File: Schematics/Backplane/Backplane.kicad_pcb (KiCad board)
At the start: 2 copper layers, 69.5 x 99 mm, 17 parts, among them J1 Edge Connector (SLOT 1), J2 Edge Connector (SLOT 2), J3 Edge Connector (SLOT 3), J4 Edge Connector (SLOT 4), J5 Edge Connector (SLOT 5)

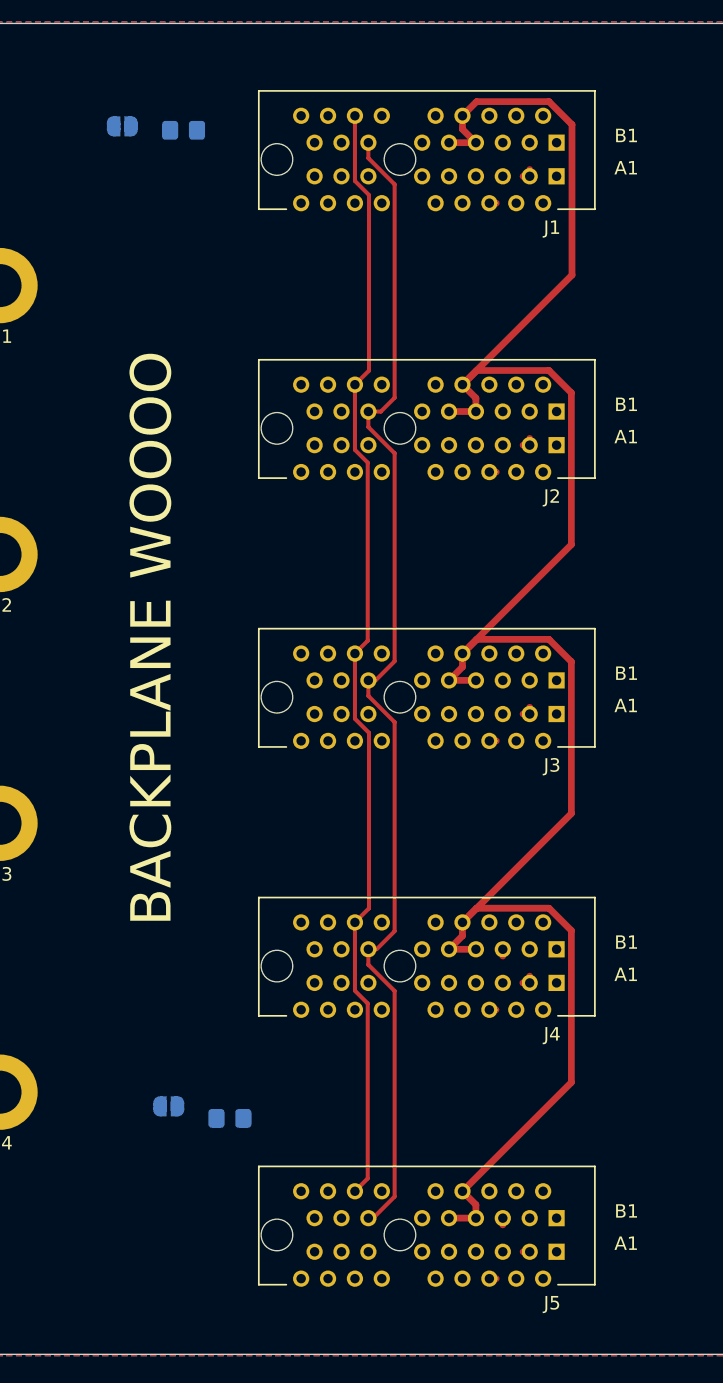
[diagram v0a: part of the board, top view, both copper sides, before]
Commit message: Tweaked slot placement on PCB
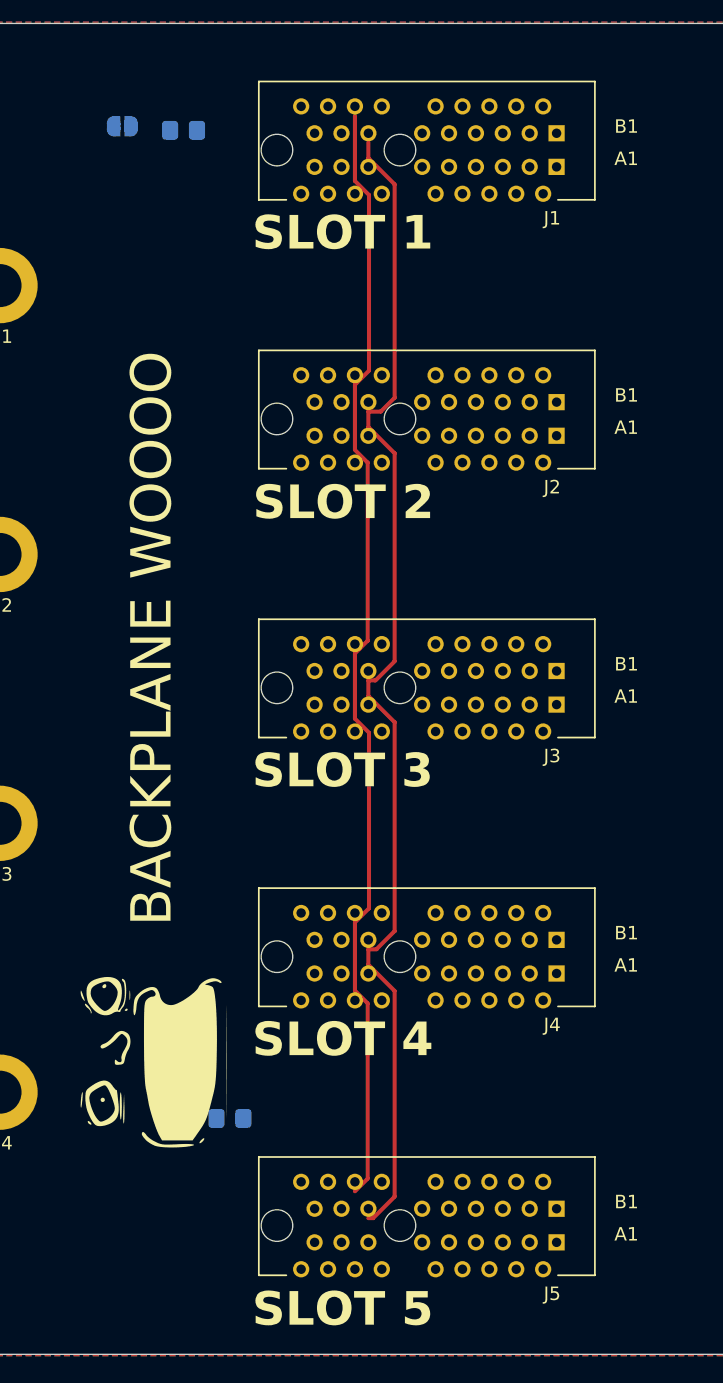
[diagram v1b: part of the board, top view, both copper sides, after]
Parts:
- moved J4 0.70 mm to (32.8, 69.4)
- moved J5 0.70 mm to (32.8, 89.4)
- moved J1 0.70 mm to (32.8, 9.42)
- moved J2 0.70 mm to (32.8, 29.4)
- moved J3 0.70 mm to (32.8, 49.4)
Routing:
- net BATT_B: track 150.0 -> 0.00 mm
- net GND1: track 8.00 -> 0.00 mm
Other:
- board text added: "SLOT 1"
- board text added: "SLOT 2"
- board text added: "SLOT 3"
- board text added: "SLOT 4"
- board text added: "SLOT 5"

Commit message: Best attempt at 2-layer PCB (incomplete)
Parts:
- removed JP1: TOP_TERMINATION, Jumper:SolderJumper-2_P1.3mm_Open_RoundedPad1.0x1.5mm
- removed JP2: BOT_TERMINATION, Jumper:SolderJumper-2_P1.3mm_Open_RoundedPad1.0x1.5mm
- R1: footprint Resistor_SMD:R_0805_2012Metric_Pad1.20x1.40mm_HandSolder -> Resistor_SMD:R_0603_1608Metric_Pad0.98x0.95mm_HandSolder
- R2: footprint Resistor_SMD:R_0805_2012Metric_Pad1.20x1.40mm_HandSolder -> Resistor_SMD:R_0603_1608Metric
- moved R2 6.97 mm to (19.6, 88.4)
- moved R1 2.56 mm to (19.2, 8.15)
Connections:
- net CAN_L renamed CAN_N
- J1 pad B14: CAN_H -> CAN_P
- J2 pad B14: CAN_H -> CAN_P
- J3 pad B14: CAN_H -> CAN_P
- J4 pad B14: CAN_H -> CAN_P
- J5 pad B14: CAN_H -> CAN_P
- R1 pad 1: Net-(JP1-A) -> CAN_P
- R2 pad 1: Net-(JP2-A) -> CAN_P
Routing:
- net BATT_B: track 0.00 -> 135.2 mm
- net 3.3V_A: track 0.00 -> 127.2 mm, vias 0 -> 4
- net GND1: track 0.00 -> 111.7 mm
- net BATT_A: track 0.00 -> 84.2 mm
- net CAN_H: track 83.3 -> 0.00 mm
- net 5.0V_A: track 0.00 -> 74.3 mm, vias 0 -> 2
- net GND2: track 0.00 -> 73.2 mm
- net 3.3V_B: track 0.00 -> 57.8 mm
- net CAN_N: track 87.9 -> 59.8 mm
- net CAN_P: track 0.00 -> 21.2 mm
- removed copper zone on F.Cu, net GND1
- removed copper zone on B.Cu, net GND2
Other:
- copper layers 2 -> 4
- board text added: "Don't use full copper pours; want PCB to be as RF-penetrable as possible"
- board text added: "MODULARIZED SYSTEMS INTERCONNECTED IN VERTICAL STACK (MSIVS) Acronym; something that describes the connected yet independent module stack"
- board text added: "Make sure to use busbars; don't want current to have to run through each connector to get from SLOT1 to SLOT5"
- board text added: "STACK INTERCONNECT GEN1"
- board text added: "Very likely going to need to do 4-layer"

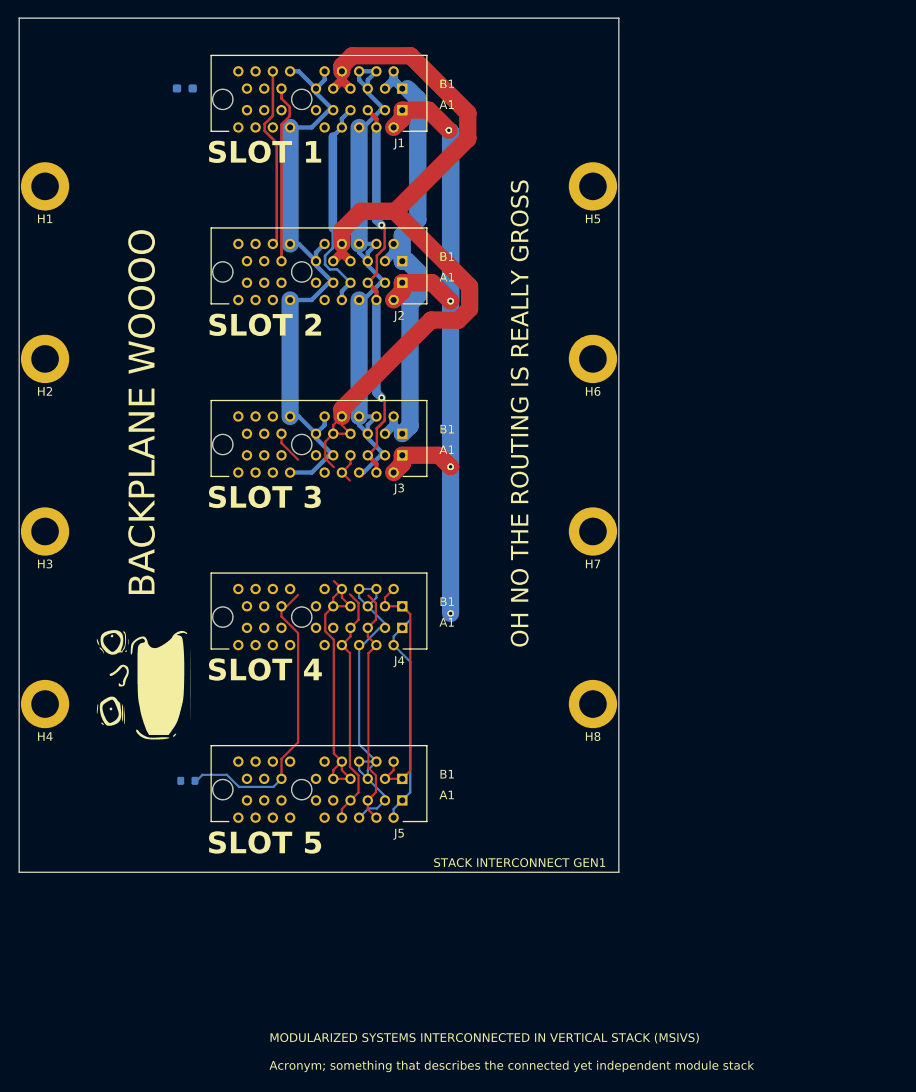
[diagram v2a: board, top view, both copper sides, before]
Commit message: Completed PCB layout (2-layer). DRC Pass.
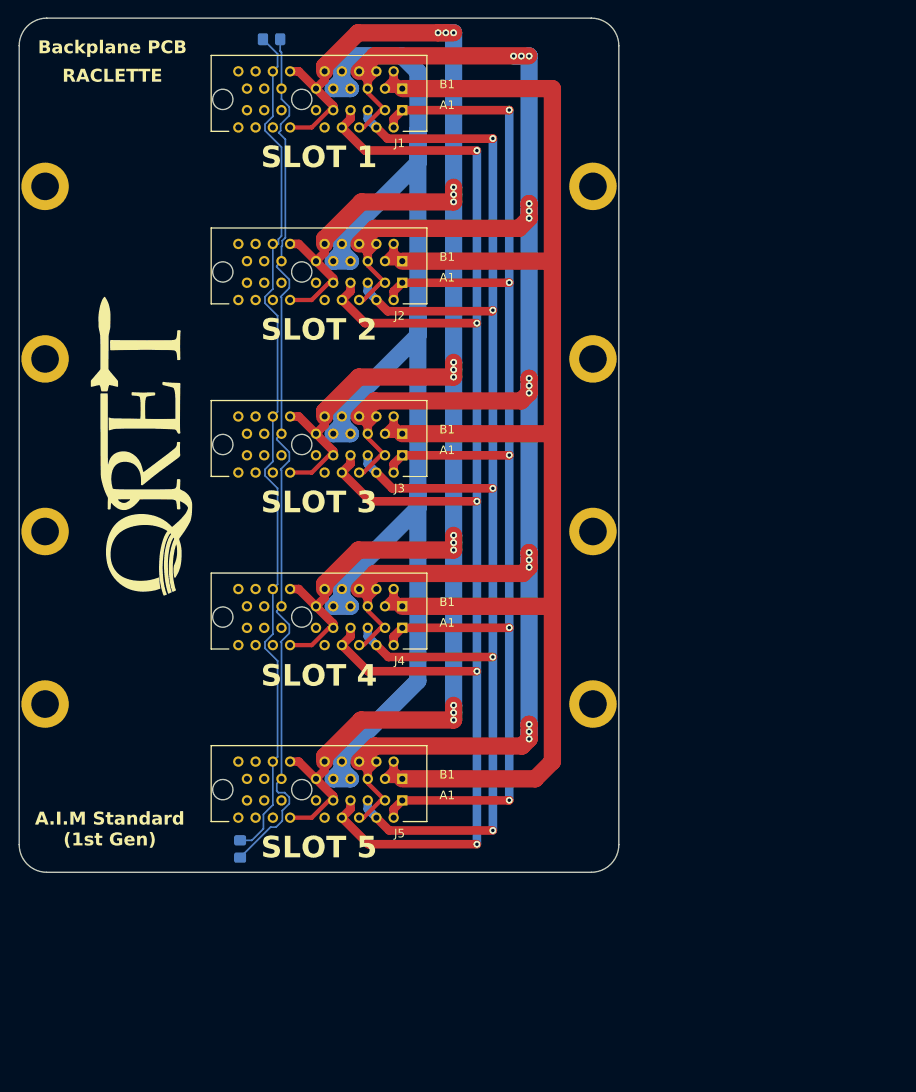
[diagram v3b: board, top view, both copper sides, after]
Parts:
- H1, H2, H3, H4, H5, H6, H7, H8: footprint MountingHole:MountingHole_3.2mm_M3_DIN965_Pad -> MountingHole:MountingHole_3.2mm_M3_ISO14580_Pad
- R1: footprint Resistor_SMD:R_0603_1608Metric_Pad0.98x0.95mm_HandSolder -> Resistor_SMD:R_0805_2012Metric_Pad1.20x1.40mm_HandSolder
- R2: footprint Resistor_SMD:R_0603_1608Metric -> Resistor_SMD:R_0805_2012Metric_Pad1.20x1.40mm_HandSolder
- moved R1 11.6 mm to (29.2, 2.45)
- moved R2 9.95 mm to (25.6, 96.3), turned to -90 degrees
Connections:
- net CAN_N renamed CAN_L
- net CAN_P renamed CAN_H
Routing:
- net GND2: track 73.2 -> 251.4 mm, vias 0 -> 15
- net GND1: track 111.7 -> 256.4 mm, vias 0 -> 15
- net 3.3V_B: track 57.8 -> 176.9 mm, vias 0 -> 5
- net BATT_A: track 84.2 -> 194.4 mm
- net 5.0V_A: track 74.3 -> 162.9 mm, vias 2 -> 5
- net CAN_H: track 21.2 -> 101.7 mm
- net CAN_L: track 59.8 -> 104.2 mm
- net BATT_B: track 135.2 -> 173.6 mm
- net 3.3V_A: track 127.2 -> 154.1 mm, vias 4 -> 5
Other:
- outline, holes or cut-outs redrawn
- copper layers 4 -> 2
- board text added: "A.I.M Standard (1st Gen)"
- board text added: "Backplane PCB"
- board text added: "RACLETTE"
- board text added: "Raclette Rev 1.0 QRET Mar 2024 Kennan Bays Owen Price"
- board text removed: "BACKPLANE WOOOO"
- board text removed: "MODULARIZED SYSTEMS INTERCONNECTED IN VERTICAL STACK (MSIVS) Acronym; something that describes the connected yet independent module stack"
- board text removed: "Make sure to use busbars; don't want current to have to run through each connector to get from SLOT1 to SLOT5"
- board text removed: "OH NO THE ROUTING IS REALLY GROSS"
- board text removed: "STACK INTERCONNECT GEN1"
- board text removed: "Very likely going to need to do 4-layer"

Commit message: Updated PCB layout to have 6th module slot
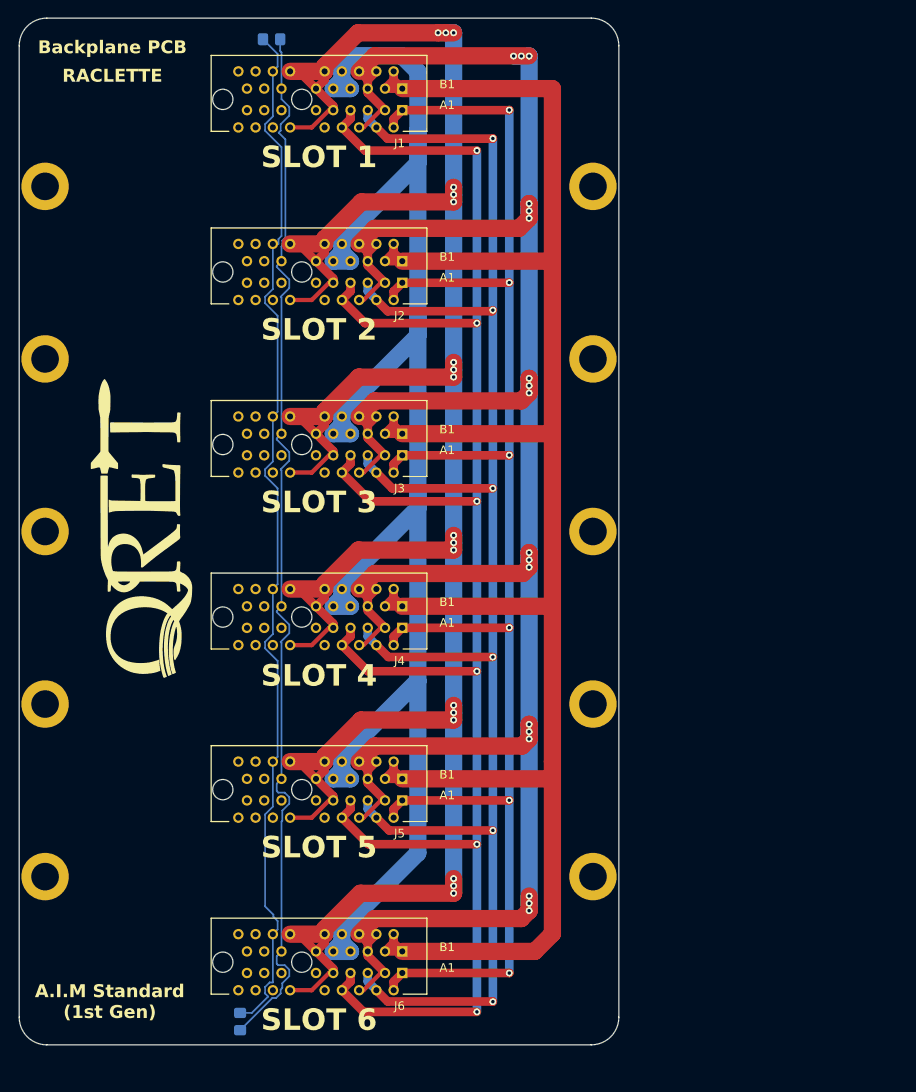
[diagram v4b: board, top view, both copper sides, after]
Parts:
- added H10: MountingHole, MountingHole:MountingHole_3.2mm_M3_ISO14580_Pad, F.Cu at (66.5, 99.5)
- added H9: MountingHole, MountingHole:MountingHole_3.2mm_M3_ISO14580_Pad, F.Cu at (3.00, 99.5)
- added J6: Edge Connector (SLOT 6), footprints:AMPHENOL_10018784-10210TLF, F.Cu at (32.8, 109.4)
- moved R2 20.0 mm to (25.6, 116.3)
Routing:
- net GND2: track 251.4 -> 329.8 mm, vias 15 -> 18
- net GND1: track 256.4 -> 311.8 mm, vias 15 -> 18
- net BATT_A: track 194.4 -> 237.6 mm
- net BATT_B: track 173.6 -> 212.4 mm
- net 3.3V_B: track 176.9 -> 215.4 mm, vias 5 -> 6
- net 5.0V_A: track 162.9 -> 199.2 mm, vias 5 -> 6
- net 3.3V_A: track 154.1 -> 189.0 mm, vias 5 -> 6
- net CAN_H: track 101.7 -> 123.4 mm
- net CAN_L: track 104.2 -> 125.7 mm
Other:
- board size 69.5 x 99 mm -> 69.5 x 119 mm
- board text added: "5-Slot V1.0 diagram"
- board text added: "Raclette Rev 1.1 QRET Feb 2025 Kennan Bays Owen Price"
- board text added: "SLOT 6"
- board text added: "Shrink distance between Modules?"
- board text removed: "Raclette Rev 1.0 QRET Mar 2024 Kennan Bays Owen Price"

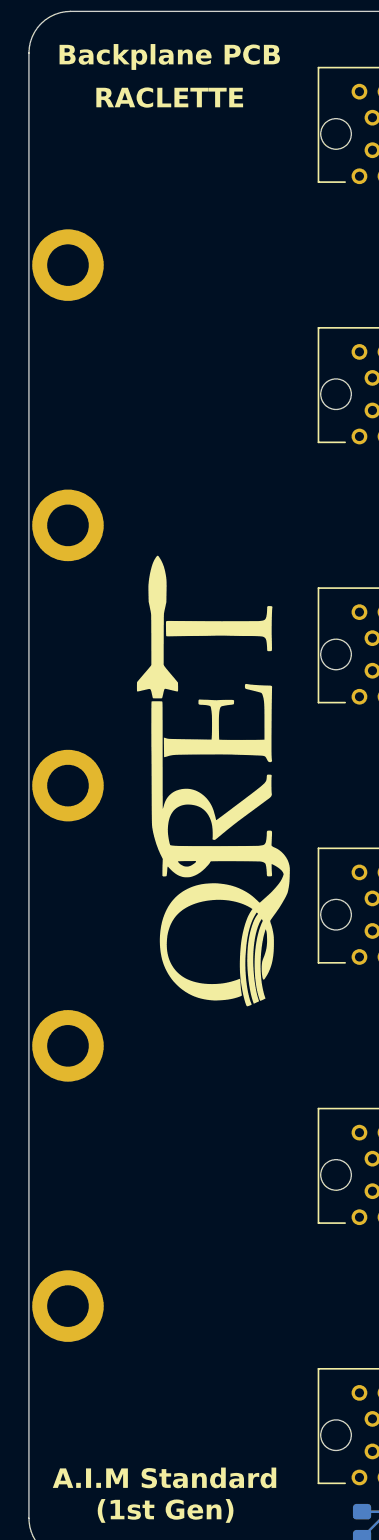
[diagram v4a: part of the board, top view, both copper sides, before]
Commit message: Tweaked silkscreen
- Added version number to RACLETTE text
- Added "PB-FREE" notice
- Updated version date
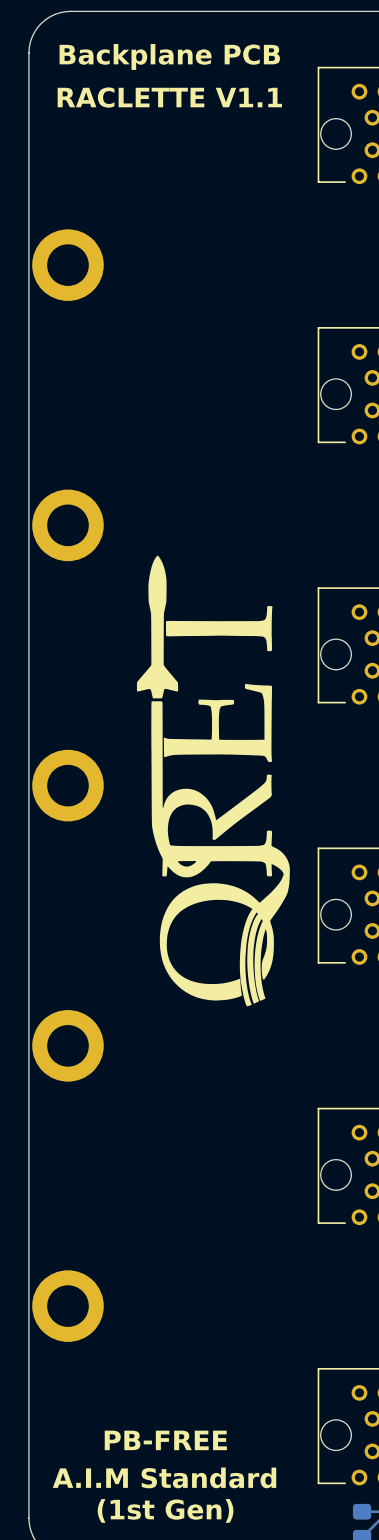
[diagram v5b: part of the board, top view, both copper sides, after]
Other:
- board text added: "PB-FREE"
- board text added: "RACLETTE V1.1"
- board text added: "Raclette Rev 1.1 QRET Mar 2025 Kennan Bays Owen Price"
- board text removed: "RACLETTE"
- board text removed: "Raclette Rev 1.1 QRET Feb 2025 Kennan Bays Owen Price"

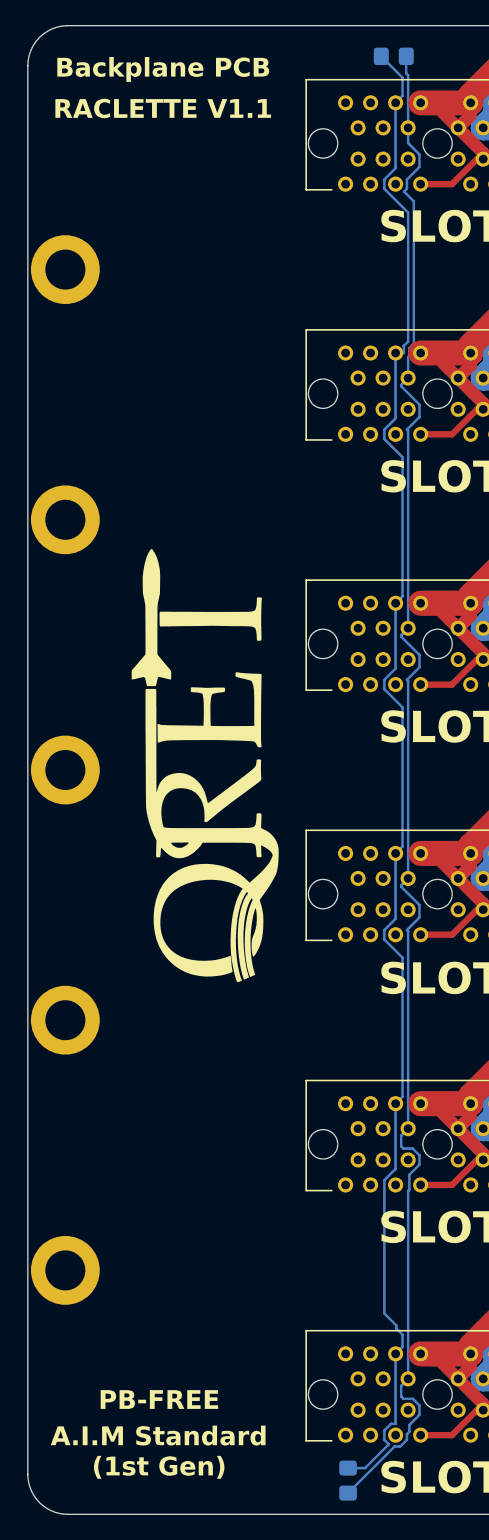
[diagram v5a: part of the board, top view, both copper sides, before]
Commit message: Added new name & tweaked silkscreen
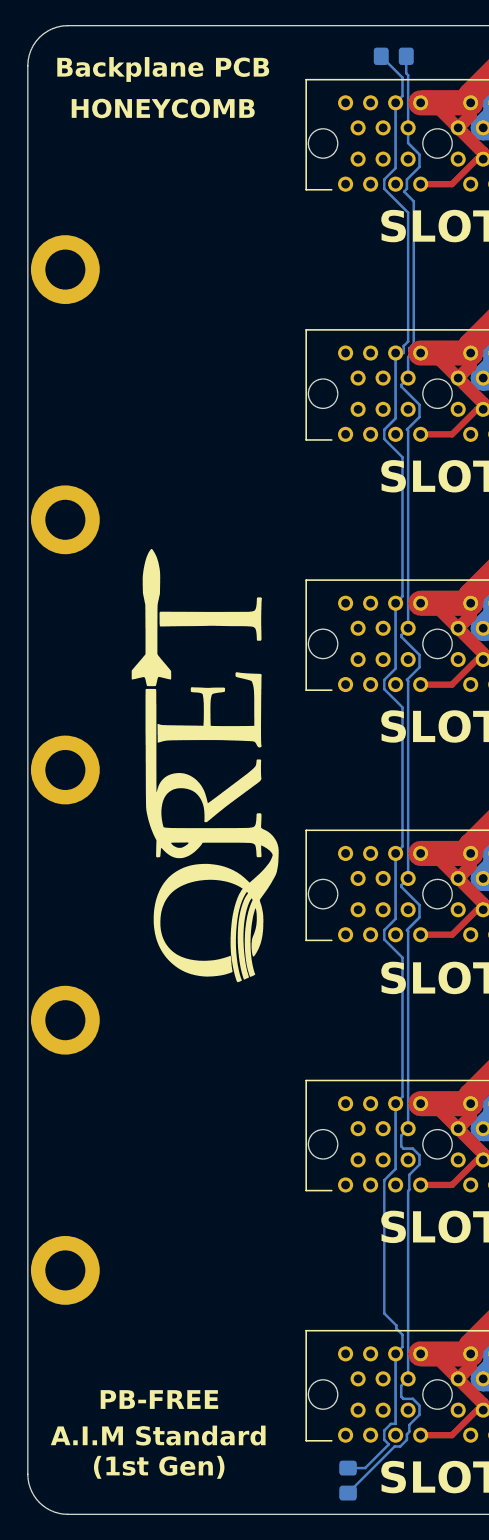
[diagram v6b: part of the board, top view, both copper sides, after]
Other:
- board text added: "Backplane PCB Rev 1.1 QRET Mar 2025 Kennan Bays Owen Price"
- board text added: "HONEYCOMB"
- board text removed: "RACLETTE V1.1"
- board text removed: "Raclette Rev 1.1 QRET Mar 2025 Kennan Bays Owen Price"
